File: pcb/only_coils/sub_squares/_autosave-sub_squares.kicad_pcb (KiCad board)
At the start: 4 copper layers, 70 x 50 mm, 10 parts, among them J2 Conn_01x06_Pin, J4 Conn_01x03_Pin

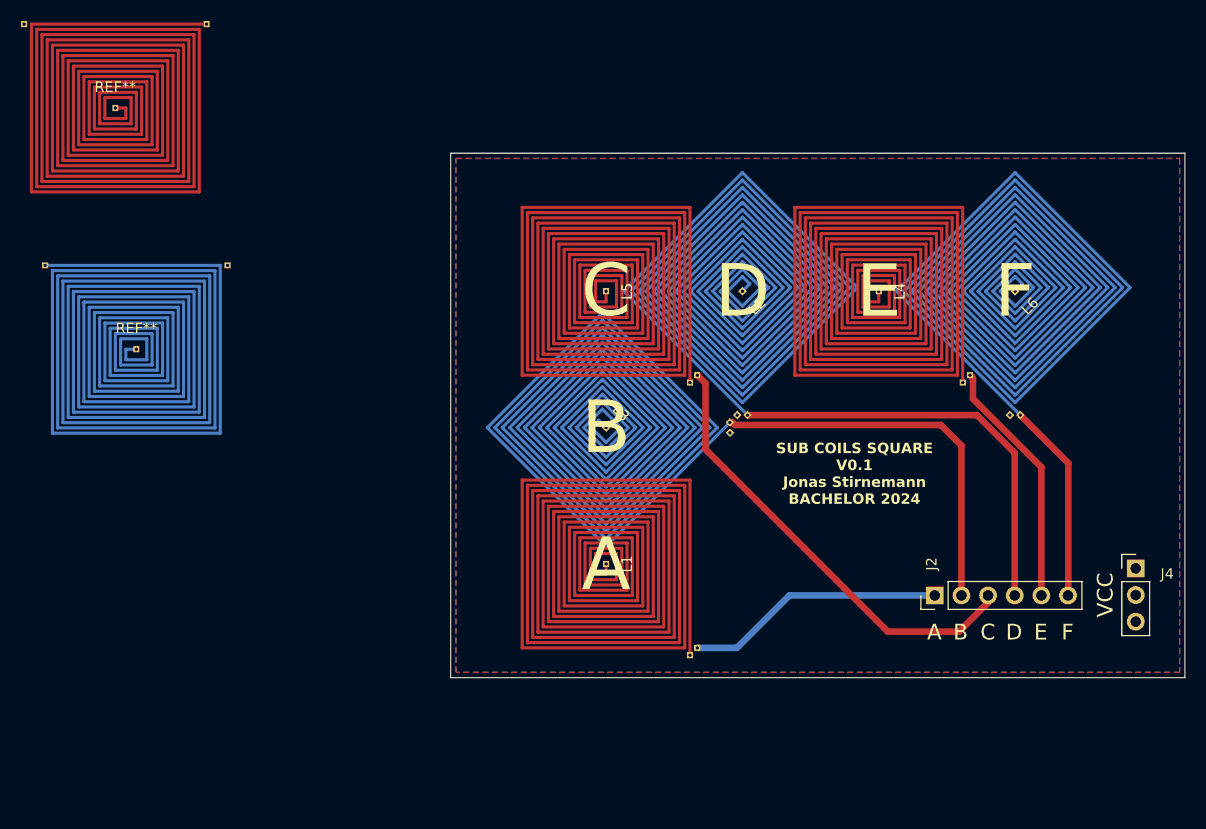
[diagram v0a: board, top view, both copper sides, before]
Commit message: Added poster pptx and pdf
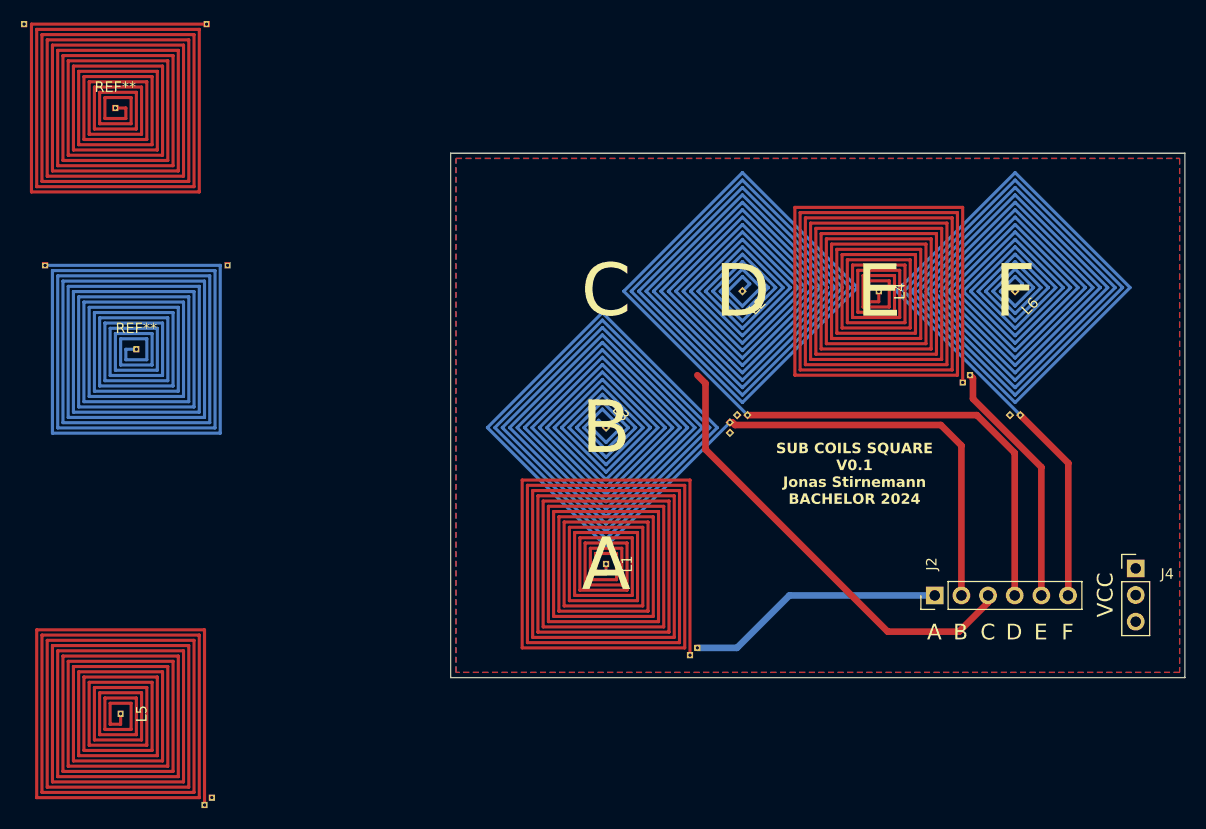
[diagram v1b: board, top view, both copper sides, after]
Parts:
- moved L5 61.4 mm to (40.0, 87.8)
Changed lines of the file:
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@@
 	(footprint "sub_coils:top_coil"
 		(layer "F.Cu")
-		(at 86.285025 47.471317 -90)
+		(at 40 87.75 -90)
 		(descr "Top Coil")
 		(property "Reference" "L5"
@@
 		)
 		(height 4)
-		(gr_text "50,0000 mm"
+		(gr_text "1968,5039 mils"
 			(at 144.31934 59.305632 90)
 			(layer "Cmts.User")
@@
 		)
 		(height -4)
-		(gr_text "70,0000 mm"
+		(gr_text "2755,9055 mils"
 			(at 106.46934 87.155632 0)
 			(layer "Cmts.User")
